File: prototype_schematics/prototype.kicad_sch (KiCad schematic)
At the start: 91 parts, among them J1 AudioJack3, J2 Conn_01x04, J3 Conn_Coaxial, U1 MAX2608EUT+T, U10 TA0411A, U2 SPX3819M5-L, U3 TLV61046ADB, U4 MAX2680AUT+, U5 CD74HC4046A, U6 BGA2802, U7 TPA721DR, U8 SPX3819M5-L-3-3, U9 PSA4-5043, Y1 ECS-96SMF21A30

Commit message: add digikey parts and replace af amp
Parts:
- removed C22: 5pF, symbol Device:C_Small
- removed R12: 100k, symbol Device:R_US
- removed U7: TPA721DR, D8, symbol TPA721DR:TPA721DR
- added C24: 24pF, symbol Device:C_Small
- added R15: 100k, symbol Device:R_US
- added R16: DNI, symbol Device:R_US
- added U7: IS31AP4991A, Package_SO:MSOP-8_3x3mm_P0.65mm, symbol Amplifier_Audio:IS31AP4991-SLS2
- C23: renamed from C25; value 1uF -> 100nF
- C26: renamed from C28; value 0.1uF -> 1uF
- C29: renamed from C27; value 1uF -> 0.47
- C9: value 1nF -> 1pF
- JP1, JP2, JP3: footprint (none) -> Jumper:SolderJumper-2_P1.3mm_Open_TrianglePad1.0x1.5mm
- U1: footprint 21-0058I_MXM -> MAX2608EUT:21-0058I_MXM; Digikey (none) -> MAX2608EUT+TCT-ND
- U10: footprint footprint:FILTER-SMD_8P-L5.0-W5.0-BL -> filter:FILTER-SMD_8P-L5.0-W5.0-BL; Digikey (none) -> 4606-TA0411ACT-ND
- U2: Digikey (none) -> 1016-1871-1-ND
- U3: Digikey (none) -> 296-47674-1-ND
- U4: footprint 21-0058I_MXM -> MAX2680:21-0058I_MXM; Digikey (none) -> 175-MAX2680AUT+TCT-ND
- U5: footprint (none) -> Package_SO:SOIC-16_3.9x9.9mm_P1.27mm; Digikey (none) -> 296-9209-5-ND
- U6: Digikey (none) -> 568-14547-1-ND
- U8: Digikey (none) -> 1016-1873-1-ND
- U9: footprint PSA4-5043_:PSA4-5043_ -> PSA4-5043:PSA4-5043; Digikey (none) -> 3157-PSA4-5043+CT-ND
- Y1: footprint ECS-96SMF21A30:XTAL_ECS-96SMF21A30 -> filter:XTAL_ECS-96SMF21A30; Digikey (none) -> X717CT-ND
- renumbered C19 to C18, C18 to C19, C23 to C22, C24 to C25, C29 to C27, C26 to C28, R13 to R10, R14 to R11, R15 to R12, R10 to R13, R11 to R14, R9 to R7, R7 to R8, R8 to R9
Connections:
- net +5V: now also U7.1 (~{SDB}), U7.6 (V+)
- net AFOUT_N: now also C24.1, R15.1, U7.5
- net AFOUT_P: now also U7.8
- net GND: now also U7.7 (GND)
- net at RV2.1: now also C23.1, RV2.2, R16.1
- net at C29.2: now also U7.2 (BYP), U7.3 (+)
- new net: C24.2, R15.2, R16.2, RV2.3, U7.4 (-)
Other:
- moved on the sheet: C18, C23, C26, C27, C29, C32, C33, C34, C35, D1, D2, D3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

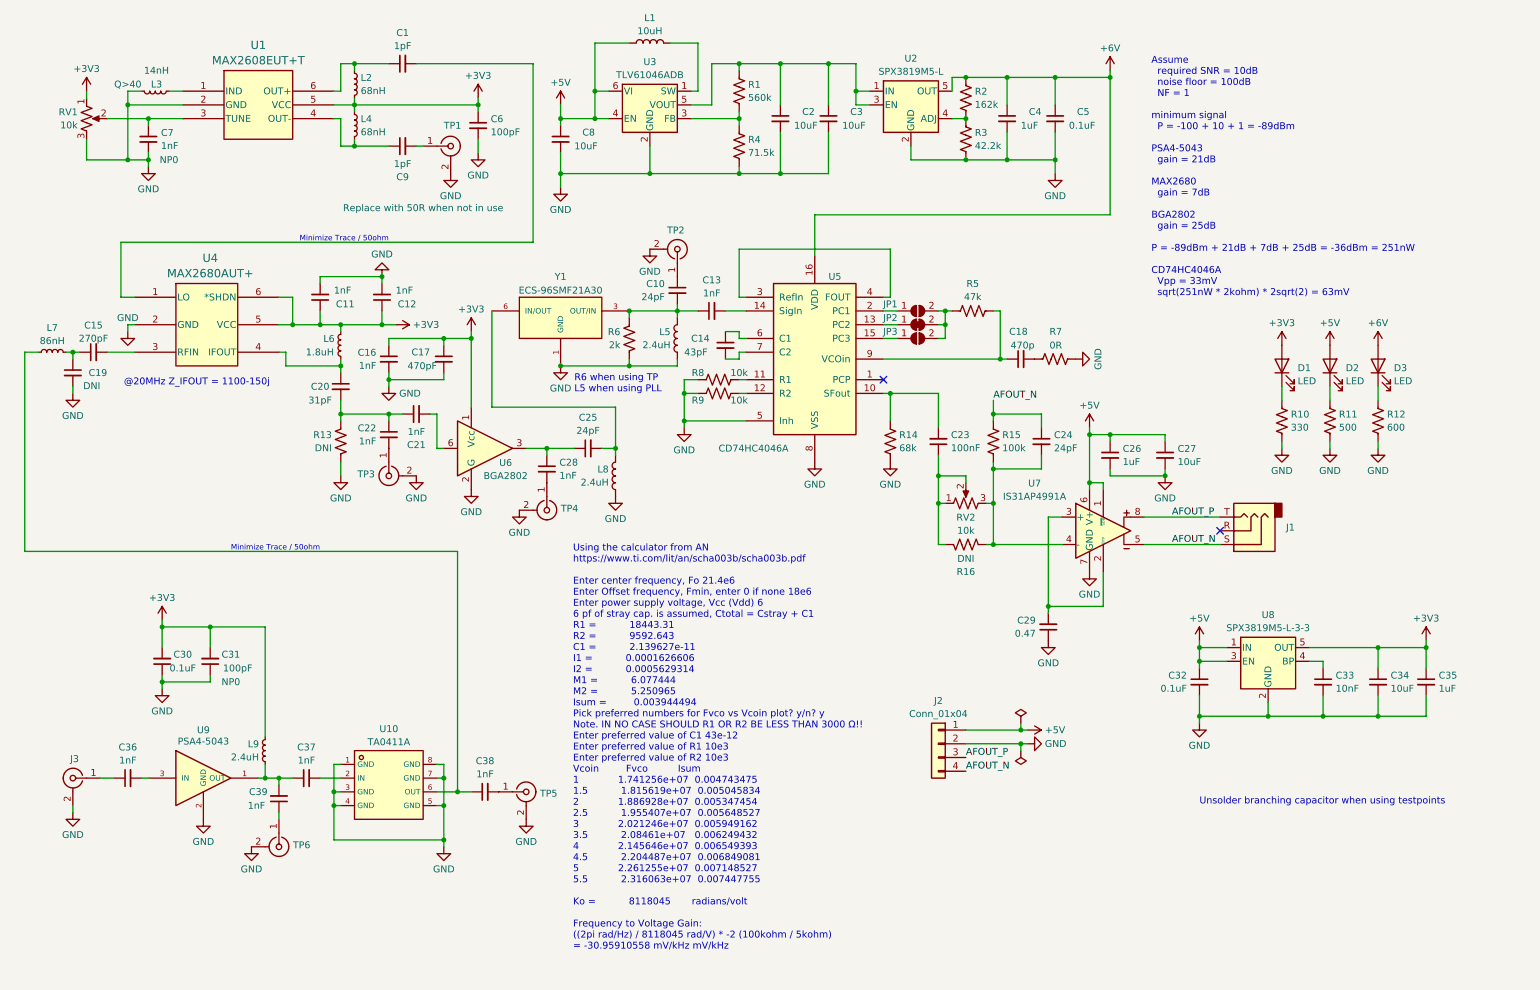
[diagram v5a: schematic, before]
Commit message: add digikey part numbers
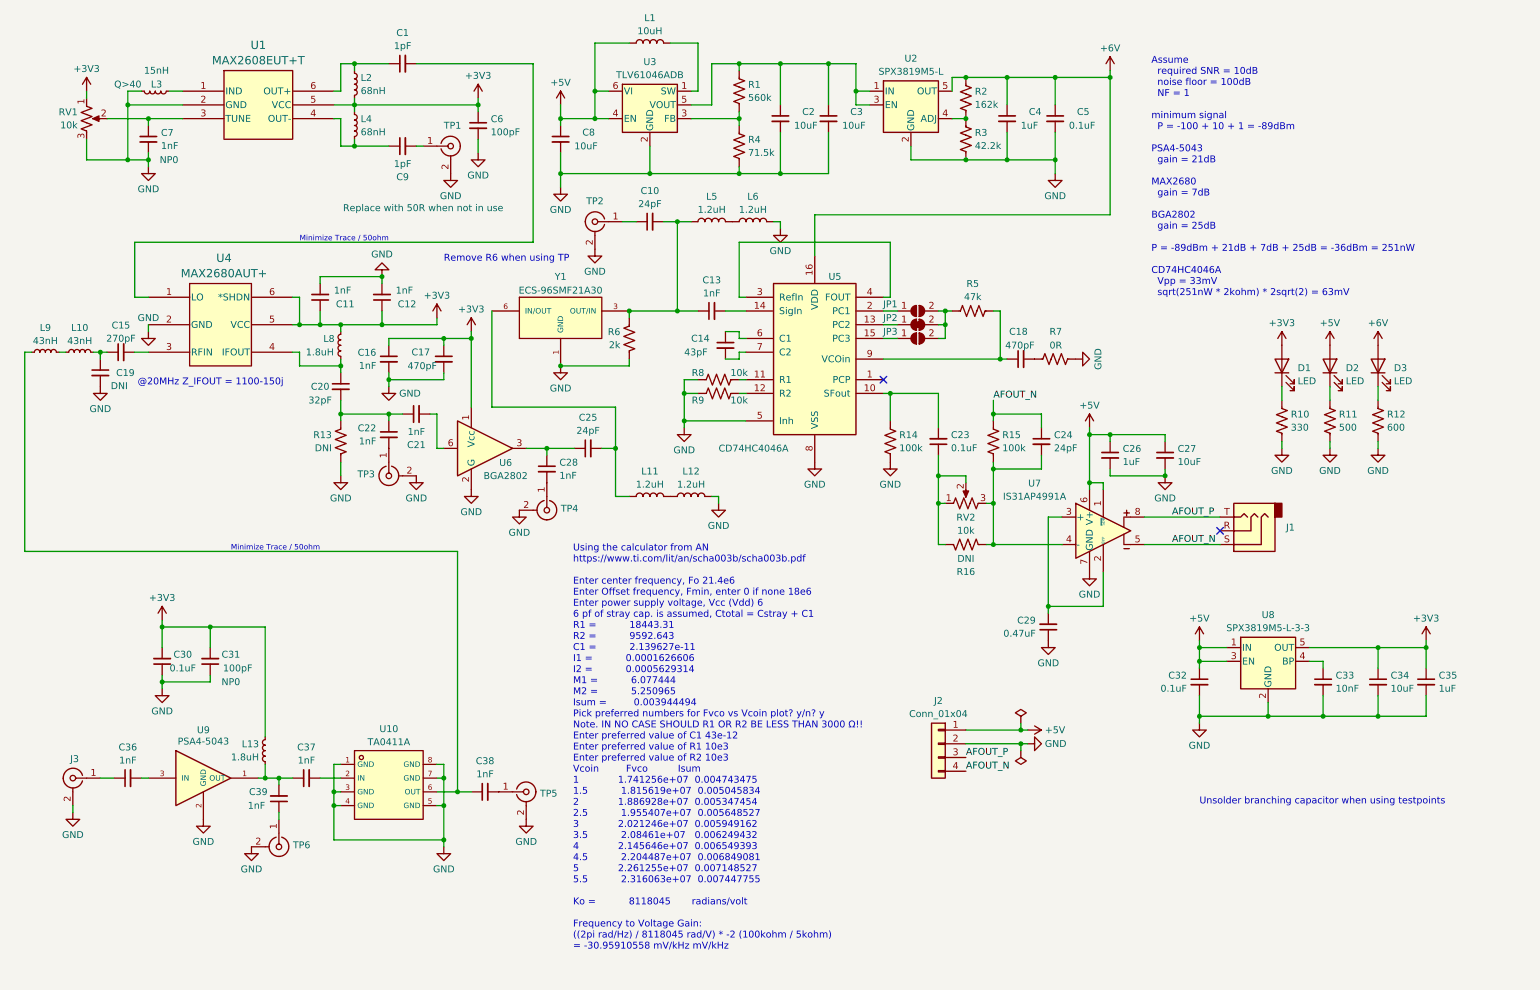
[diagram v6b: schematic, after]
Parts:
- removed L8: 2.4uH, symbol Device:L
- added L11, L12, L6: 1.2uH, symbol Device:L
- added L9: 43nH, symbol Device:L_Small
- C1, C9: Digikey (none) -> 490-16342-1-ND
- C11, C12, C13, C16, C21, C22, C28, C36, C37, C38, C39, C7: Digikey (none) -> 4713-GMC10CG102F50NTCT-ND
- C14: Digikey (none) -> 490-GCM1885C2A430FA16DCT-ND
- C15: Digikey (none) -> 490-16410-1-ND
- C17: Digikey (none) -> 399-C0603C471F8HAC7867CT-ND
- C18: value 470p -> 470pF; Digikey (none) -> 399-C0603C471F8HAC7867CT-ND
- C20: value 31pF -> 32pF; Digikey (none) -> 478-06031A320FAT2ACT-ND
- C23: value 100nF -> 0.1uF
- C29: value 0.47 -> 0.47uF; Digikey (none) -> 1276-2082-1-ND
- C31, C6: Digikey (none) -> 720-1649-1-ND
- C33: Digikey (none) -> 490-4781-1-ND
- L1: footprint (none) -> Inductor_SMD:L_0805_2012Metric_Pad1.15x1.40mm_HandSolder; Digikey (none) -> 587-2045-1-ND
- L10: renamed from L7; value 86nH -> 43nH; Digikey (none) -> 490-6892-1-ND
- L13: renamed from L9; value 2.4uH -> 1.8uH; Digikey (none) -> 553-BWCS002928211R8G00CT-ND
- L2, L4: Digikey (none) -> 712-LRW0805WJ68NGG001ECT-ND
- L3: value 14nH -> 15nH; Digikey (none) -> 490-1171-1-ND
- L5: value 2.4uH -> 1.2uH; Digikey (none) -> 2035-1186-1-ND
- L8: renamed from L6; Digikey (none) -> 553-BWCS002928211R8G00CT-ND
- R14: value 68k -> 100k
- TP1, TP2, TP3, TP4, TP5, TP6: Digikey (none) -> 343-CONMHF1-SMD-TCT-ND
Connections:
- net GND: now also L12.2, L6.2; no longer L5.2
- net at C38.1, U10.6 (OUT): now also L9.1; no longer L10.1
- net at C25.2, Y1.6 (IN/OUT): now also L11.1
- new net: L5.2, L6.1
- new net: L10.1, L9.2
- new net: L11.2, L12.1
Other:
- note added: "Remove R6 when using TP"
- note removed: "R6 when using TP L5 when using PLL"
- moved on the sheet: C15, C19, L10, TP2, U4

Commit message: add more digikey part numbers
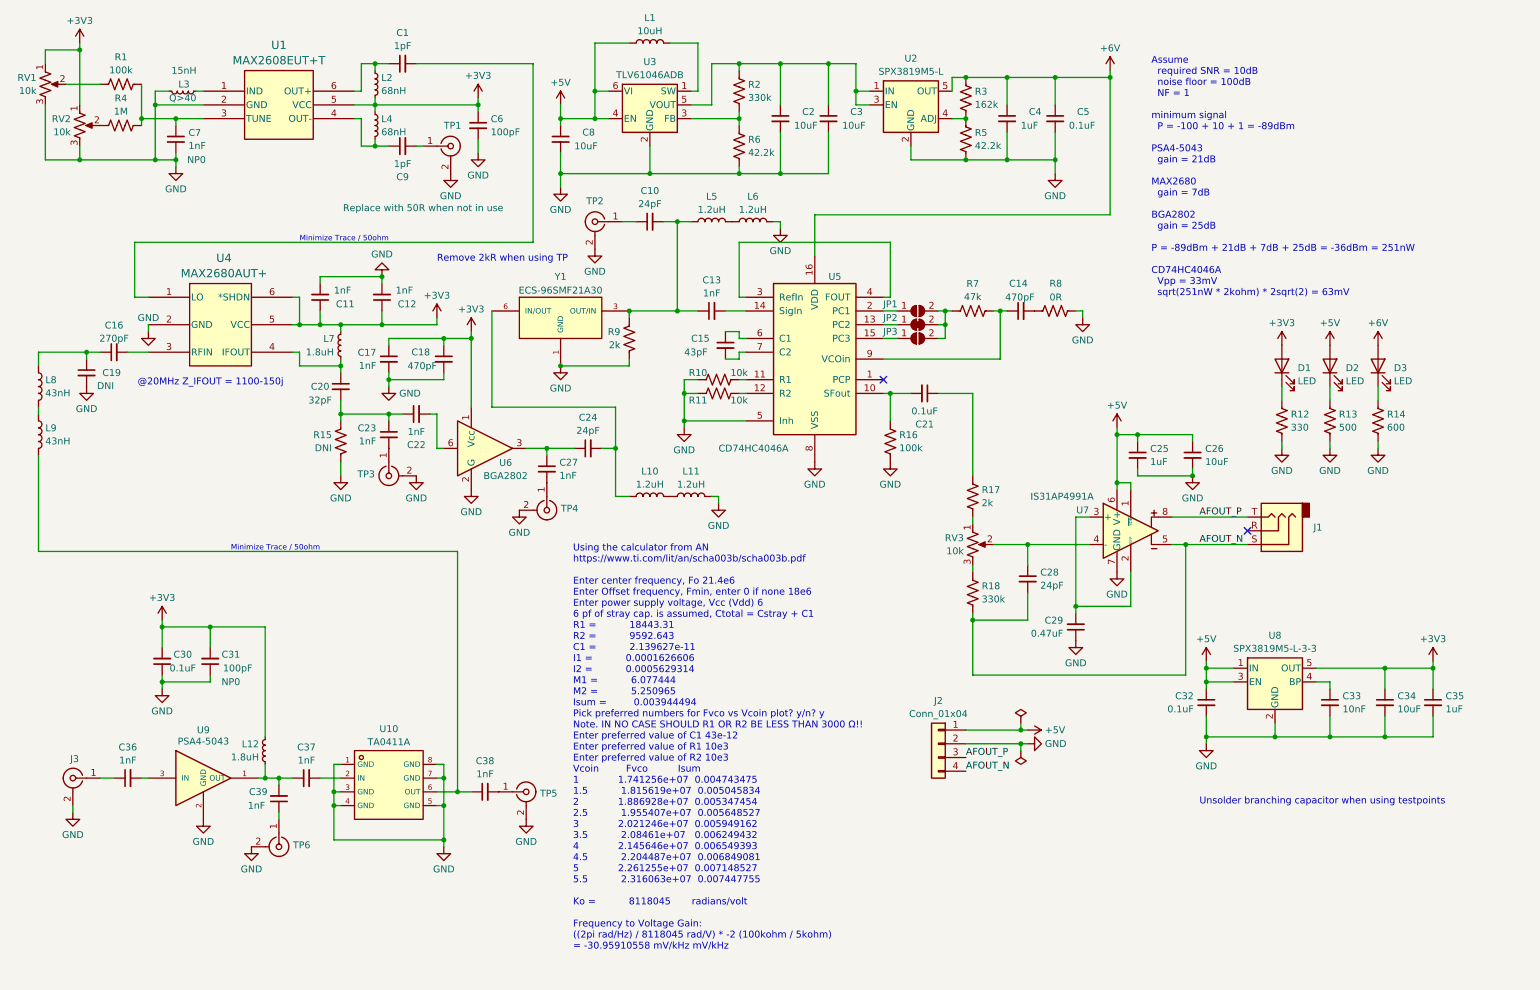
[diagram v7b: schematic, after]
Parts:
- removed C24: 24pF, symbol Device:C_Small
- removed L10, L9: 43nH, symbol Device:L_Small
- removed R15: 100k, symbol Device:R_US
- removed R16: DNI, symbol Device:R_US
- added C28: 24pF, symbol Device:C_Small
- added L8, L9: 43nH, symbol Device:L
- added R1: 100k, symbol Device:R_US
- added R17: 2k, symbol Device:R_US
- added R18: 330k, symbol Device:R_US
- added R4: 1M, symbol Device:R_US
- added RV3: 10k, symbol Device:R_Potentiometer_US
- C10: Digikey (none) -> 13-CC0603FRNPO9BN240CT-ND
- C24: renamed from C25; Digikey (none) -> 13-CC0603FRNPO9BN240CT-ND
- J1: Digikey (none) -> CP1-2503A-ND
- R2: renamed from R1; value 560k -> 330k; Digikey (none) -> 311-330KCRCT-ND
- R3: renamed from R2; Digikey (none) -> RMCF0805FT162KCT-ND
- R5: renamed from R3; Digikey (none) -> 311-42.2KCRCT-ND
- R6: renamed from R4; value 71.5k -> 42.2k; Digikey (none) -> 311-42.2KCRCT-ND
- R7: renamed from R5; Digikey (none) -> 311-47.0KCRCT-ND
- R9: renamed from R6; Digikey (none) -> RMCF0805FT2K00CT-ND
- renumbered C18 to C14, C14 to C15, C15 to C16, C16 to C17, C17 to C18, C23 to C21, C21 to C22, C22 to C23, C26 to C25, C27 to C26, C28 to C27, L11 to L10, L12 to L11, L13 to L12, L8 to L7, R8 to R10, R9 to R11, R10 to R12, R11 to R13, R12 to R14, R13 to R15, R14 to R16, R7 to R8
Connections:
- net +3V3: now also RV2.1
- net AFOUT_N: now also C28.2, R18.2
- net GND: now also RV2.3
- net at C38.1, U10.6 (OUT): now also L9.2
- net at C16.1, C19.1: now also L8.1
- net at U7.4 (-): now also C28.1, RV3.2; no longer RV2.3
- net at C7.1, U1.3 (TUNE): now also R1.2, R4.2; no longer RV1.2
- new net: R4.1, RV2.2
- new net: R18.1, RV3.3
- new net: R17.2, RV3.1
- new net: L8.2, L9.1
- new net: R1.1, RV1.2
- new net: C21.1, R17.1
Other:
- note added: "Remove 2kR when using TP"
- note removed: "Remove R6 when using TP"
- moved on the sheet: C14, C16, C19, C21, C25, C26, C29, C32, C33, C34, C35, C7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

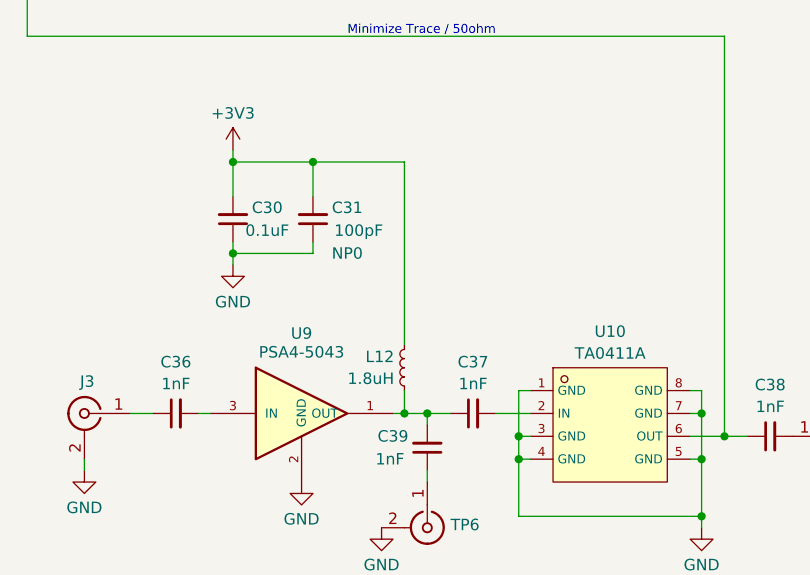
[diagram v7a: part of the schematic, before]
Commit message: finish sourcing and footprints
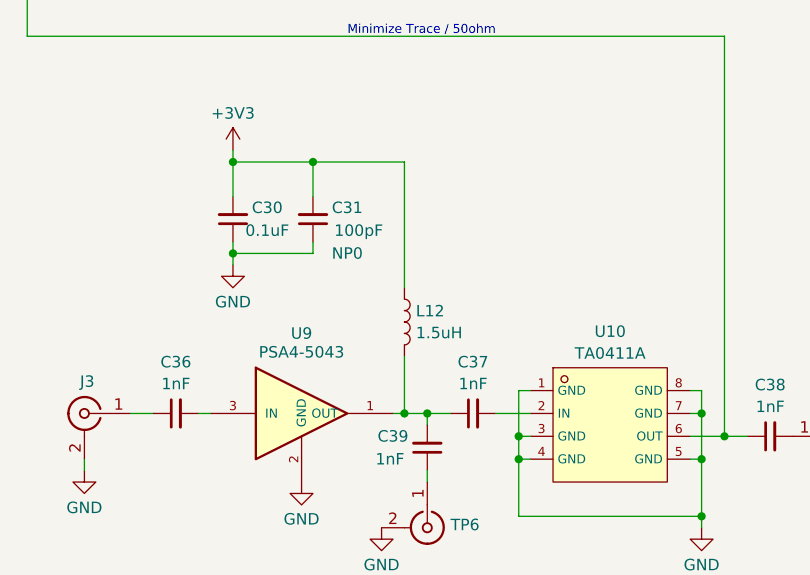
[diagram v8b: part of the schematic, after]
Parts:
- removed L12: 1.8uH, symbol Device:L_Small
- added L12: 1.5uH, Inductor_SMD:L_0201_0603Metric_Pad0.64x0.40mm_HandSolder, symbol Device:L
- C1, C10, C11, C12, C13, C14, C15, C16, C17, C18, C19, C20, C22, C23, C24, C27, C28, C31, C36, C37, C38, C39, C6, C7, C9: footprint (none) -> Capacitor_SMD:C_0603_1608Metric_Pad1.08x0.95mm_HandSolder
- C2, C21, C25, C26, C29, C3, C30, C32, C33, C34, C35, C4, C5, C8: footprint (none) -> Capacitor_SMD:C_0805_2012Metric_Pad1.18x1.45mm_HandSolder
- D1, D2, D3: footprint (none) -> LED_SMD:LED_1206_3216Metric_Pad1.42x1.75mm_HandSolder
- J1: footprint (none) -> SJ1_2503A:CONN_SJ1-2503A
- J2: footprint (none) -> Connector_JST:JST_PH_S4B-PH-K_1x04_P2.00mm_Horizontal
- J3: footprint (none) -> Connector_Coaxial:SMA_Wurth_60312002114503_Vertical
- L10, L11, L2, L4, L5, L6: footprint (none) -> Inductor_SMD:L_0805_2012Metric_Pad1.15x1.40mm_HandSolder
- L3, L8, L9: footprint (none) -> Inductor_SMD:L_0603_1608Metric_Pad1.05x0.95mm_HandSolder
- L7: footprint (none) -> Inductor_SMD:L_0805_2012Metric_Pad1.15x1.40mm_HandSolder; Digikey 553-BWCS002928211R8G00CT-ND -> 445-MLF2012A1R8JT000CT-ND
- R1, R10, R11, R12, R13, R14, R15, R16, R17, R18, R2, R3, R4, R5, R6, R7, R8, R9: footprint (none) -> Resistor_SMD:R_0805_2012Metric_Pad1.20x1.40mm_HandSolder
- RV1, RV2, RV3: footprint (none) -> TRIM_PT01:TRIM_PT01-D120K2-B103; Digikey (none) -> 2223-PT01-B120D-B103-ND
- TP1, TP2, TP3, TP4, TP5, TP6: footprint (none) -> CONMHF1_SMD_T:CONN_CONMHF1-SMD_LNX
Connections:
- net +3V3: now also L12.1
- net at C37.1, C39.2, U9.1 (OUT): now also L12.2
